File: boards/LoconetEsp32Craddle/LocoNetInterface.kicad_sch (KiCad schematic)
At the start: 18 parts, among them J2 RJ12, J3 RJ12, Q1 SS8050, Q2 SS8050, U1 LM311

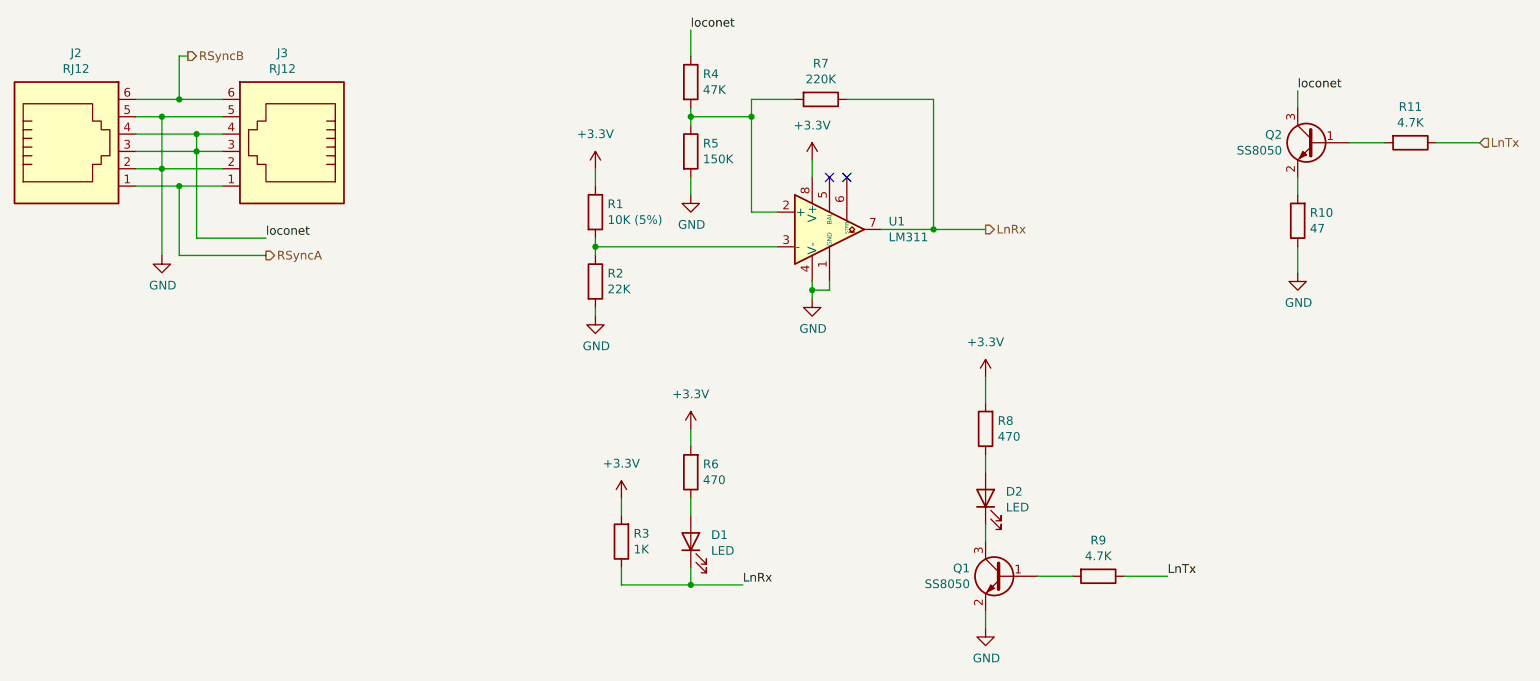
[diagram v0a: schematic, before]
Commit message: Update a Kicad 10 y eliminacion ERC
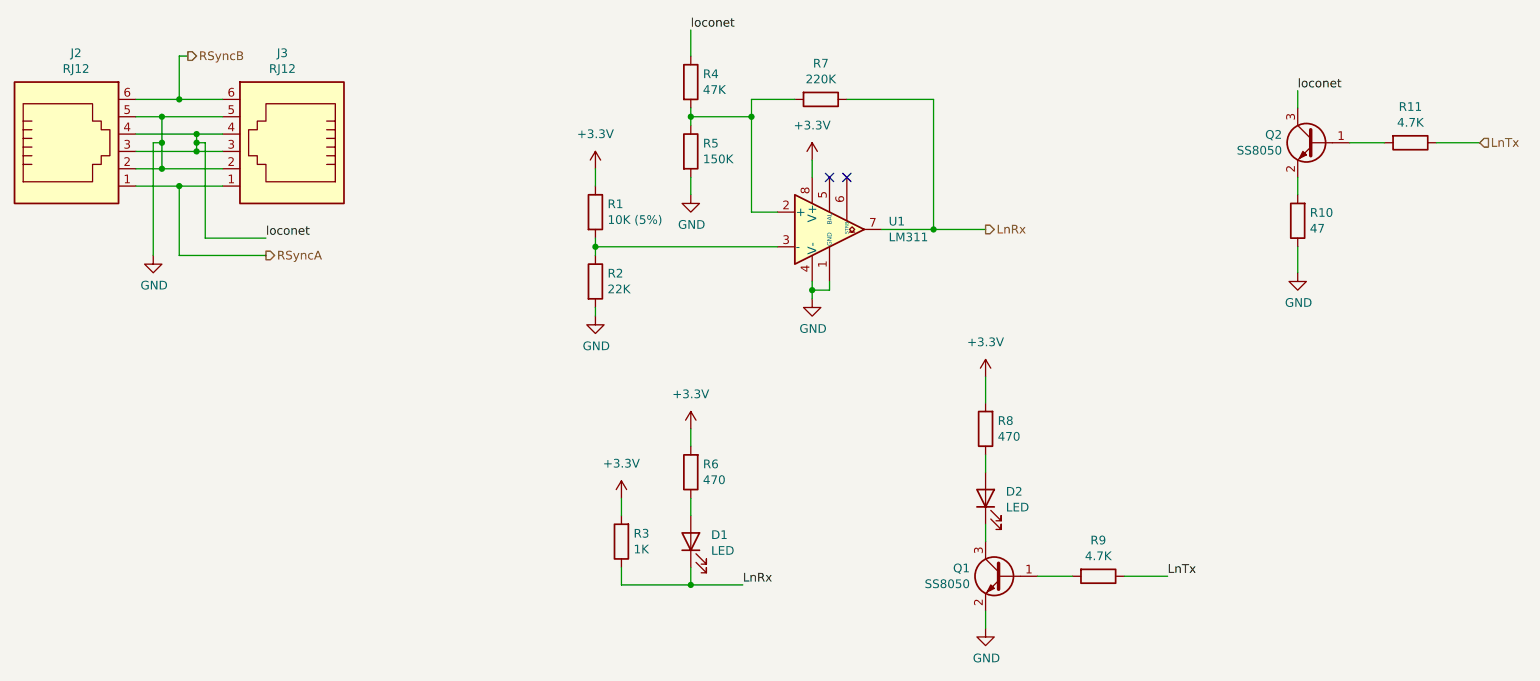
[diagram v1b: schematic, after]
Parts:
- J2, J3: footprint LocoNetInterface:AMPHENOL_RJE0166001 -> LocoNetInterface:RJ12_AMPHENOL_RJE0166001
- Q1, Q2: symbol Device:Q_NPN_BEC -> Transistor_BJT:SS8050
